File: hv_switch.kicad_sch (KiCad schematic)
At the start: 11 parts, among them IC3 MAX14802CCM+, IC7 ISO7641FMDWR

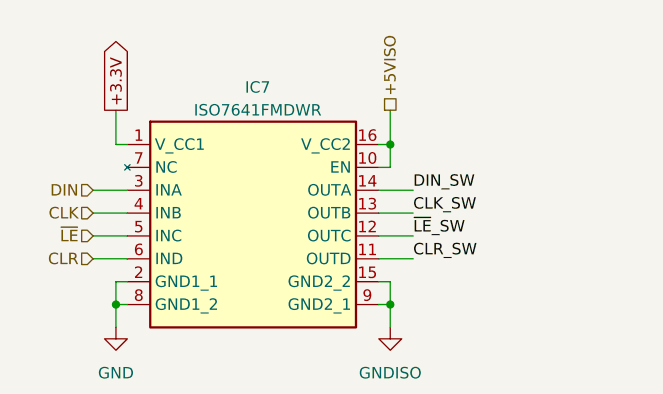
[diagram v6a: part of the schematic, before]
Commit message: fix: update names for IC components
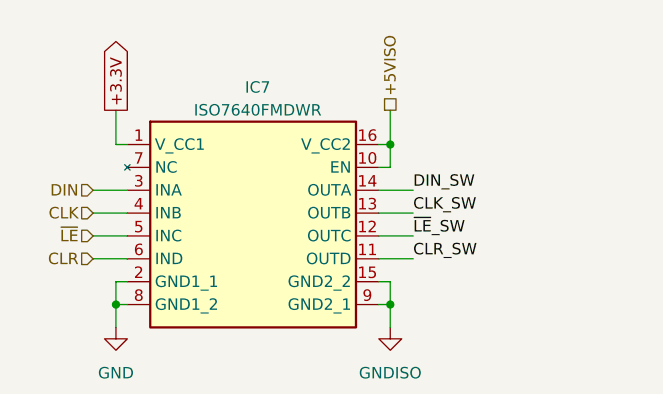
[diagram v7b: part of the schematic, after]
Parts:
- IC7: value ISO7641FMDWR -> ISO7640FMDWR
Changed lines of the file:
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@@
 			)
 		)
-		(property "Value" "ISO7641FMDWR"
+		(property "Value" "ISO7640FMDWR"
 			(at 38.608 22.86 0)
 			(effects
